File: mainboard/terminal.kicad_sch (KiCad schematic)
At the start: 67 parts, among them J2 Conn_01x04, Q5 MPS3704, Y1 14.31818 MHz

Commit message: additional footprint work
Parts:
- CR1, CR2, CR3, CR4: footprint mainboard:apple-1_D_DO-35_SOD27_P10.16mm_Horizontal -> mainboard:apple-1_D_DO-35_SOD27_P10.16mm_Horizontal_altarrow
- Q5: footprint (none) -> mainboard:apple-1_TO-92_HandSolder
- R12: footprint (none) -> mainboard:apple-1_R_Axial_DIN0207_L6.3mm_D2.5mm_P10.16mm_Horizontal
- renumbered CAP1 to C1, CAP2 to C2, CAP3 to C3, CAP4 to C4, CAP5 to C5, CAP6 to C6, CAP7 to C7, C10 to C_IC10, C12 to C_IC12, C13 to C_IC13, C14 to C_IC14, C15 to C_IC15, C3 to C_IC3, C4 to C_IC4, C5 to C_IC5, C6 to C_IC6, C7 to C_IC7, C8 to C_IC8, C9 to C_IC9

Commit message: added graphicard
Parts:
- C7: footprint (none) -> mainboard:CP_Axial_25u
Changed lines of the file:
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@@
 			)
 		)
-		(property "Footprint" ""
+		(property "Footprint" "mainboard:CP_Axial_25u"
 			(at 248.92 350.52 0)
 			(hide yes)

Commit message: mainboard work
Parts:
- R12: footprint mainboard:apple-1_R_Axial_DIN0207_L6.3mm_D2.5mm_P10.16mm_Horizontal -> mainboard:apple-1_Potentiometer_Bourns_3329H_Vertical
- Y1: footprint Crystal:Resonator-2Pin_W10.0mm_H5.0mm -> mainboard:apple-1_Crystal_HC49-U_Vertical
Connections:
- net GND: now also R12.3; no longer R12.1
- net at Q5.1 (E): now also R12.1; no longer R12.3
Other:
- moved on the sheet: R12
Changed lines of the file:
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@@
 			)
 		)
-		(property "Footprint" "Crystal:Resonator-2Pin_W10.0mm_H5.0mm"
+		(property "Footprint" "mainboard:apple-1_Crystal_HC49-U_Vertical"
 			(at 72.39 365.76 0)
 			(hide yes)
@@
 	(symbol
 		(lib_id "Device:R_POT")
-		(at 137.16 251.46 180)
+		(at 137.16 251.46 0)
+		(mirror y)
 		(unit 1)
 		(body_style 1)
@@
 		(dnp no)
 		(property "Reference" "R12"
-			(at 138.938 250.2916 0)
+			(at 138.938 252.6284 0)
 			(show_name no)
 			(do_not_autoplace no)
@@
 		)
 		(property "Value" "100"
-			(at 138.938 252.603 0)
+			(at 138.938 250.317 0)
 			(show_name no)
 			(do_not_autoplace no)
@@
 			)
 		)
-		(property "Footprint" "mainboard:apple-1_R_Axial_DIN0207_L6.3mm_D2.5mm_P10.16mm_Horizontal"
+		(property "Footprint" "mainboard:apple-1_Potentiometer_Bourns_3329H_Vertical"
 			(at 137.16 251.46 0)
 			(hide yes)

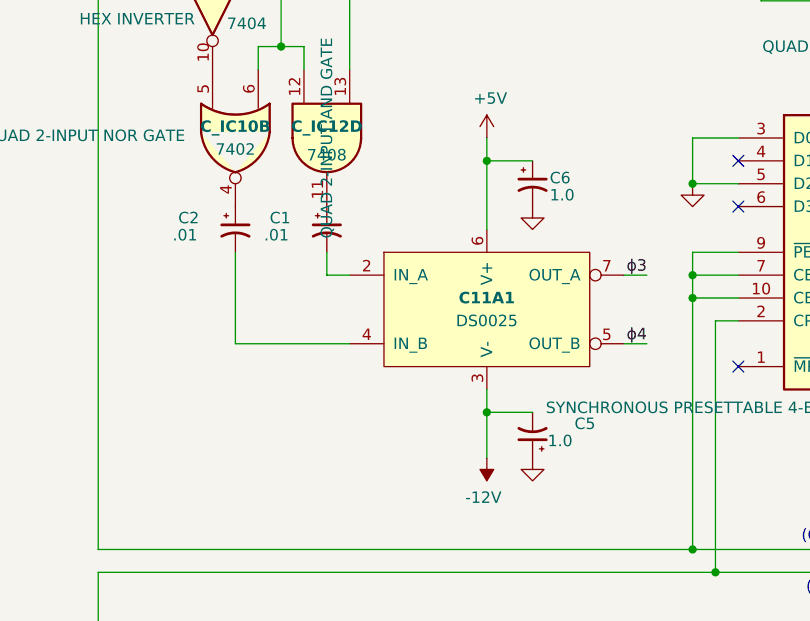
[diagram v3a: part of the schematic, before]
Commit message: added kicad drawing template
new file:   boardfont.svg
new file:   img/00101P3.png
new file:   mainboard/apple1template.kicad_wks
additional work on mainboard
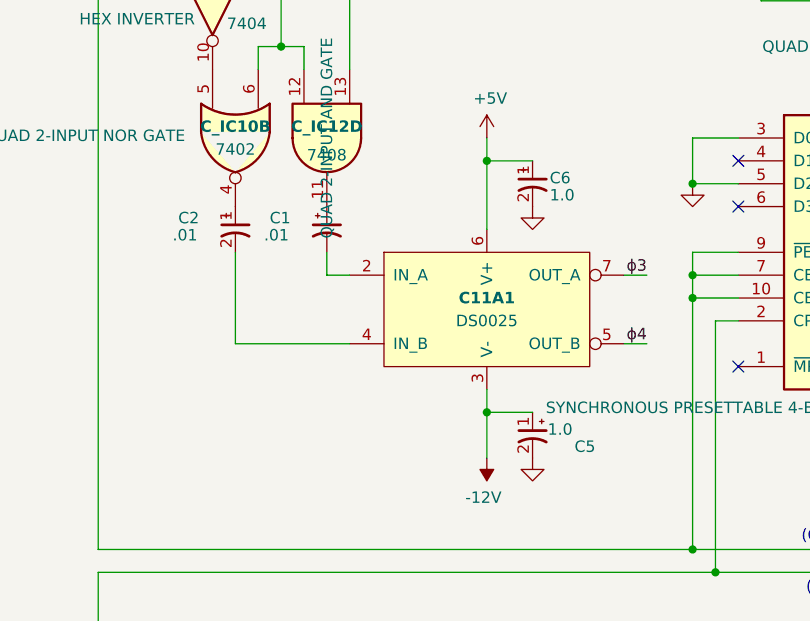
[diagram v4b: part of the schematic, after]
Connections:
- net -12V: now also C5.1; no longer C5.2
- net GND: now also C5.2; no longer C5.1
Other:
- title: Apple I - Terminal Section -> Processor Section
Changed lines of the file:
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@@
 	(paper "C")
 	(title_block
-		(title "Apple I - Terminal Section")
+		(title "Processor Section")
 		(date "2019-08-11")
 		(comment 1 "Drawn by Nicolas Robin")
@@
 	)
 	(symbol
+		(lib_name "CP1_Small_3")
 		(lib_id "Device:CP1_Small")
 		(at 50.8 167.64 0)
@@
 	)
 	(symbol
+		(lib_name "CP1_Small_1")
 		(lib_id "Device:CP1_Small")
-		(at 83.82 190.5 180)
+		(at 83.82 190.5 0)
+		(mirror y)
 		(unit 1)
 		(body_style 1)
@@
 		(dnp no)
 		(property "Reference" "C5"
-			(at 90.805 189.23 0)
+			(at 90.805 191.77 0)
 			(show_name no)
 			(do_not_autoplace no)
@@
 		)
 		(property "Value" "1.0"
-			(at 88.265 191.135 0)
+			(at 88.265 189.865 0)
 			(show_name no)
 			(do_not_autoplace no)
@@
 	)
 	(symbol
+		(lib_name "CP1_Small_2")
 		(lib_id "Device:CP1_Small")
 		(at 83.82 162.56 0)

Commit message: board is now complete, cleanup work can begin
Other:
- title: Processor Section -> Apple I - Processor Section
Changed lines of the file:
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@@
 	(paper "C")
 	(title_block
-		(title "Processor Section")
+		(title "Apple I - Processor Section")
 		(date "2019-08-11")
 		(comment 1 "Drawn by Nicolas Robin")
